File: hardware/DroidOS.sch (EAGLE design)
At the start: 17 parts, among them J1 AUDIO_JACK_3.5MM_KIT, Q1 BC337

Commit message: Changed layout
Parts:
- J1: value AUDIO_JACK_3.5MM_KIT -> AUDIO_JACK_3.5MM
- U$1: value TEENSY_LC_DIL -> TEENSY_LC
- VREG: value (none) -> 5V
- renumbered + to VBAT+, - to VBAT-
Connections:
- net N$1 renamed DAC_R
- net N$10 renamed AUD_RX
- net N$11 renamed AUD_TX
- net N$12 renamed PWM2_SIG
- net N$13 renamed PWM4_SIG
- net N$14 renamed CTRL_SIG
- net N$15 renamed PWM3_SIG
- net N$16 renamed SBUS_INV_IN
- net N$18 renamed SBUS_INV_OUT
- net N$4 renamed SPK_R
- net N$5 renamed SBUS_OUT
- net N$6 renamed 3V+
- net N$7 renamed SPK_L
- net N$9 renamed PWM1_SIG
- removed net N$2: J1.TSH, U$2.DAC_L
- new net DAC_L: J1.TIP, U$2.DAC_L
- net GND: now also J1.SLEEVE, PWM4.3; no longer J1.RSH

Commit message: v0.3
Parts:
- added PWR_SW: (no value), SparkFun-Connectors:CONN_02
- added R4: (no value), resistor:R-US_R0805
- added STATUS: (no value), led:LEDSML0805
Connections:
- new net N$1: PWR_SW.2, U$1.VIN
- new net N$2: R4.1, STATUS.A
- new net STATUS_LED: R4.2, U$1.21/A7
- net 5V: now also PWR_SW.1; no longer U$1.VIN
- net GND: now also STATUS.C
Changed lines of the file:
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@@
 </variantdefs>
 <classes>
-<class number="0" name="default" width="0.254" drill="0.381">
+<class number="0" name="default" width="0.3556" drill="0.381">
 <clearance class="0" value="0.254"/>
 </class>
@@
 <part name="PWM3" library="SparkFun-Connectors" library_urn="urn:adsk.eagle:library:513" deviceset="CONN_03" device="" package3d_urn="urn:adsk.eagle:package:38063/1"/>
 <part name="SIG_SEL" library="SparkFun-Connectors" library_urn="urn:adsk.eagle:library:513" deviceset="CONN_03" device="" package3d_urn="urn:adsk.eagle:package:38063/1"/>
+<part name="PWR_SW" library="SparkFun-Connectors" library_urn="urn:adsk.eagle:library:513" deviceset="CONN_02" device="" package3d_urn="urn:adsk.eagle:package:38039/1"/>
+<part name="STATUS" library="led" library_urn="urn:adsk.eagle:library:259" deviceset="LED" device="SML0805" package3d_urn="urn:adsk.eagle:package:15830/1"/>
+<part name="GND4" library="supply1" library_urn="urn:adsk.eagle:library:371" deviceset="GND" device=""/>
+<part name="R4" library="resistor" library_urn="urn:adsk.eagle:library:348" deviceset="R-US_" device="R0805" package3d_urn="urn:adsk.eagle:package:26059/1"/>
 </parts>
 <sheets>
@@
 <instance part="PWM3" gate="J$1" x="55.88" y="27.94" rot="R180"/>
 <instance part="SIG_SEL" gate="J$1" x="71.12" y="27.94" rot="R180"/>
+<instance part="PWR_SW" gate="G$1" x="-66.04" y="17.78"/>
+<instance part="STATUS" gate="G$1" x="17.78" y="111.76" rot="R90"/>
+<instance part="GND4" gate="1" x="30.48" y="111.76" rot="R90"/>
+<instance part="R4" gate="G$1" x="7.62" y="111.76" rot="R180"/>
 </instances>
 <busses>
@@
 <wire x1="104.14" y1="88.9" x2="104.14" y2="83.82" width="0.1524" layer="91"/>
 </segment>
+<segment>
+<pinref part="STATUS" gate="G$1" pin="C"/>
+<pinref part="GND4" gate="1" pin="GND"/>
+<wire x1="22.86" y1="111.76" x2="27.94" y2="111.76" width="0.1524" layer="91"/>
+</segment>
 </net>
 <net name="VBAT" class="1">
@@
 <wire x1="40.64" y1="5.08" x2="22.86" y2="5.08" width="0.1524" layer="91"/>
 <wire x1="22.86" y1="5.08" x2="-55.88" y2="5.08" width="0.1524" layer="91"/>
-<wire x1="-55.88" y1="5.08" x2="-55.88" y2="33.02" width="0.1524" layer="91"/>
-<pinref part="U$1" gate="G$1" pin="VIN"/>
-<wire x1="-55.88" y1="33.02" x2="-50.8" y2="33.02" width="0.1524" layer="91"/>
 <wire x1="22.86" y1="27.94" x2="22.86" y2="5.08" width="0.1524" layer="91"/>
 <junction x="22.86" y="5.08"/>
@@
 <pinref part="PWM2" gate="J$1" pin="2"/>
 <pinref part="PWM3" gate="J$1" pin="2"/>
+<pinref part="PWR_SW" gate="G$1" pin="1"/>
+<wire x1="-58.42" y1="17.78" x2="-55.88" y2="17.78" width="0.1524" layer="91"/>
+<wire x1="-55.88" y1="17.78" x2="-55.88" y2="5.08" width="0.1524" layer="91"/>
 </segment>
 </net>
@@
 </segment>
 </net>
+<net name="N$1" class="0">
+<segment>
+<pinref part="PWR_SW" gate="G$1" pin="2"/>
+<pinref part="U$1" gate="G$1" pin="VIN"/>
+<wire x1="-58.42" y1="20.32" x2="-50.8" y2="20.32" width="0.1524" layer="91"/>
+<wire x1="-50.8" y1="20.32" x2="-50.8" y2="33.02" width="0.1524" layer="91"/>
+</segment>
+</net>
+<net name="STATUS_LED" class="0">
+<segment>
+<wire x1="2.54" y1="111.76" x2="0" y2="111.76" width="0.1524" layer="91"/>
+<wire x1="0" y1="111.76" x2="0" y2="83.82" width="0.1524" layer="91"/>
+<pinref part="U$1" gate="G$1" pin="21/A7"/>
+<wire x1="0" y1="83.82" x2="-5.08" y2="83.82" width="0.1524" layer="91"/>
+<pinref part="R4" gate="G$1" pin="2"/>
+</segment>
+</net>
+<net name="N$2" class="0">
+<segment>
+<pinref part="STATUS" gate="G$1" pin="A"/>
+<wire x1="15.24" y1="111.76" x2="12.7" y2="111.76" width="0.1524" layer="91"/>
+<pinref part="R4" gate="G$1" pin="1"/>
+</segment>
+</net>

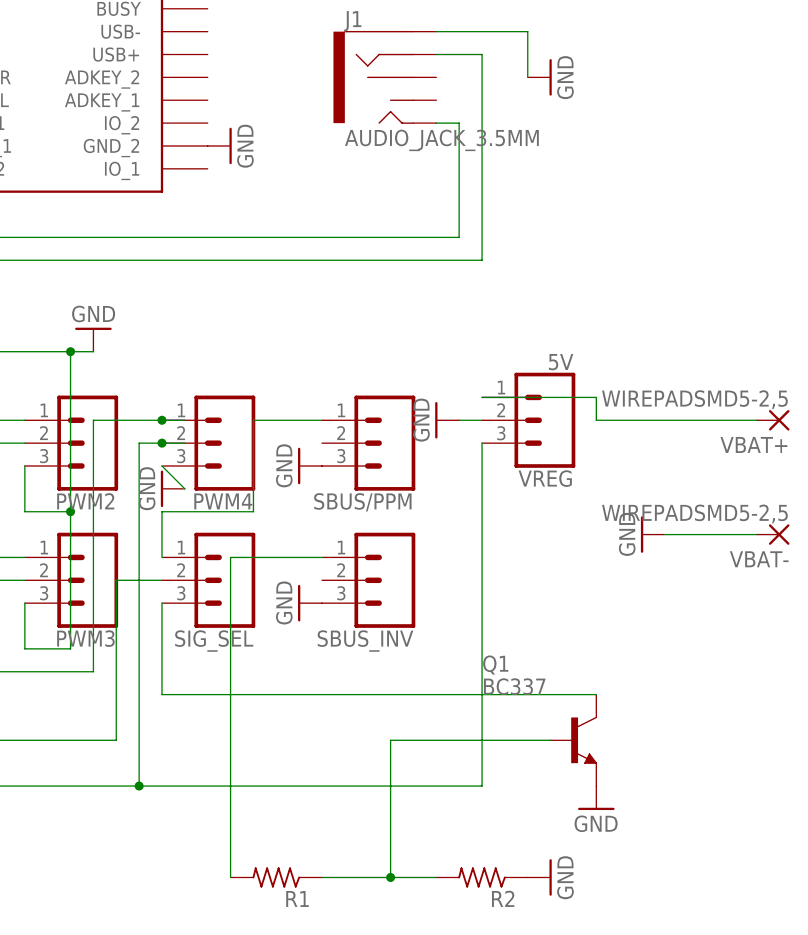
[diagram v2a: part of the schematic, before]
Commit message: Added SBUS power out
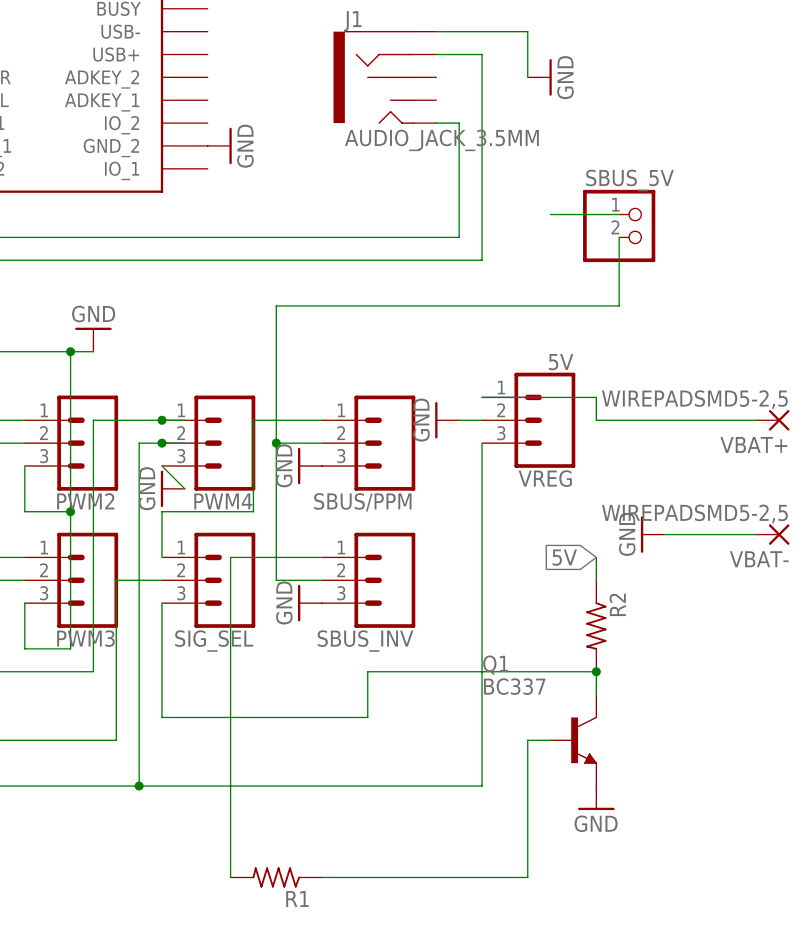
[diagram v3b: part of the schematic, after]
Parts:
- added SBUS_5V: (no value), pinhead:PINHD-1X2
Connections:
- removed net N$17: Q1.B, R1.1, R2.2
- new net N$3: SBUS/PPM.2, SBUS_5V.2, SBUS_INV.2
- new net N$4: Q1.B, R1.1
- net 5V: now also R2.1, SBUS_5V.1
- net GND: no longer R2.1
- net SBUS_INV_OUT: now also R2.2
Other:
- moved on the sheet: R2
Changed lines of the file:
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@@
 <?xml version="1.0" encoding="utf-8"?>
 <!DOCTYPE eagle SYSTEM "eagle.dtd">
-<eagle version="8.4.0">
+<eagle version="8.4.3">
 <drawing>
 <settings>
@@
 <part name="R2" library="resistor" library_urn="urn:adsk.eagle:library:348" deviceset="R-US_" device="R0805" package3d_urn="urn:adsk.eagle:package:26059/1"/>
 <part name="Q1" library="transistor-npn" library_urn="urn:adsk.eagle:library:398" deviceset="BC337*" device="" package3d_urn="urn:adsk.eagle:package:28974/2"/>
-<part name="GND9" library="supply1" library_urn="urn:adsk.eagle:library:371" deviceset="GND" device=""/>
 <part name="GND15" library="supply1" library_urn="urn:adsk.eagle:library:371" deviceset="GND" device=""/>
 <part name="VBAT+" library="wirepad" library_urn="urn:adsk.eagle:library:412" deviceset="WIREPAD" device="SMD5-2,5" package3d_urn="urn:adsk.eagle:package:30845/1"/>
@@
 <part name="GND4" library="supply1" library_urn="urn:adsk.eagle:library:371" deviceset="GND" device=""/>
 <part name="R4" library="resistor" library_urn="urn:adsk.eagle:library:348" deviceset="R-US_" device="R0805" package3d_urn="urn:adsk.eagle:package:26059/1"/>
+<part name="SBUS_5V" library="pinhead" library_urn="urn:adsk.eagle:library:325" deviceset="PINHD-1X2" device="" package3d_urn="urn:adsk.eagle:package:22435/2"/>
 </parts>
 <sheets>
@@
 <instance part="GND8" gate="1" x="78.74" y="25.4" rot="R270"/>
 <instance part="R1" gate="G$1" x="76.2" y="-5.08" rot="R180"/>
-<instance part="R2" gate="G$1" x="99.06" y="-5.08" rot="R180"/>
+<instance part="R2" gate="G$1" x="111.76" y="22.86" rot="R270"/>
 <instance part="Q1" gate="G$1" x="109.22" y="10.16"/>
-<instance part="GND9" gate="1" x="106.68" y="-5.08" rot="R90"/>
 <instance part="GND15" gate="1" x="111.76" y="2.54"/>
 <instance part="VBAT+" gate="G$1" x="132.08" y="45.72" rot="R180"/>
@@
 <instance part="GND4" gate="1" x="30.48" y="111.76" rot="R90"/>
 <instance part="R4" gate="G$1" x="7.62" y="111.76" rot="R180"/>
+<instance part="SBUS_5V" gate="G$1" x="116.84" y="66.04"/>
 </instances>
 <busses>
@@
 <pinref part="GND12" gate="1" pin="GND"/>
 <wire x1="-48.26" y1="40.64" x2="-50.8" y2="40.64" width="0.1524" layer="91"/>
-</segment>
-<segment>
-<pinref part="R2" gate="G$1" pin="1"/>
-<pinref part="GND9" gate="1" pin="GND"/>
 </segment>
 <segment>
@@
 <wire x1="-55.88" y1="17.78" x2="-55.88" y2="5.08" width="0.1524" layer="91"/>
 </segment>
+<segment>
+<pinref part="SBUS_5V" gate="G$1" pin="1"/>
+<wire x1="114.3" y1="68.58" x2="106.68" y2="68.58" width="0.1524" layer="91"/>
+</segment>
+<segment>
+<pinref part="R2" gate="G$1" pin="1"/>
+<wire x1="111.76" y1="27.94" x2="111.76" y2="30.48" width="0.1524" layer="91"/>
+<label x="111.76" y="30.48" size="1.778" layer="95" rot="R180" xref="yes"/>
+</segment>
 </net>
 <net name="PWM1_SIG" class="0">
@@
 </segment>
 </net>
-<net name="N$17" class="0">
-<segment>
-<pinref part="R1" gate="G$1" pin="1"/>
+<net name="SBUS_INV_OUT" class="0">
+<segment>
+<wire x1="63.5" y1="12.7" x2="63.5" y2="25.4" width="0.1524" layer="91"/>
+<pinref part="SIG_SEL" gate="J$1" pin="3"/>
 <pinref part="R2" gate="G$1" pin="2"/>
-<wire x1="81.28" y1="-5.08" x2="88.9" y2="-5.08" width="0.1524" layer="91"/>
-<wire x1="88.9" y1="-5.08" x2="93.98" y2="-5.08" width="0.1524" layer="91"/>
-<wire x1="88.9" y1="-5.08" x2="88.9" y2="10.16" width="0.1524" layer="91"/>
-<junction x="88.9" y="-5.08"/>
-<pinref part="Q1" gate="G$1" pin="B"/>
-<wire x1="88.9" y1="10.16" x2="106.68" y2="10.16" width="0.1524" layer="91"/>
-</segment>
-</net>
-<net name="SBUS_INV_OUT" class="0">
-<segment>
 <pinref part="Q1" gate="G$1" pin="C"/>
-<wire x1="111.76" y1="15.24" x2="63.5" y2="15.24" width="0.1524" layer="91"/>
-<wire x1="63.5" y1="15.24" x2="63.5" y2="25.4" width="0.1524" layer="91"/>
-<pinref part="SIG_SEL" gate="J$1" pin="3"/>
+<wire x1="111.76" y1="17.78" x2="111.76" y2="15.24" width="0.1524" layer="91"/>
+<wire x1="111.76" y1="17.78" x2="86.36" y2="17.78" width="0.1524" layer="91"/>
+<junction x="111.76" y="17.78"/>
+<wire x1="86.36" y1="17.78" x2="86.36" y2="12.7" width="0.1524" layer="91"/>
+<wire x1="86.36" y1="12.7" x2="63.5" y2="12.7" width="0.1524" layer="91"/>
 </segment>
 </net>
@@
 </segment>
 </net>
+<net name="N$3" class="0">
+<segment>
+<pinref part="SBUS_5V" gate="G$1" pin="2"/>
+<wire x1="114.3" y1="66.04" x2="114.3" y2="58.42" width="0.1524" layer="91"/>
+<wire x1="114.3" y1="58.42" x2="76.2" y2="58.42" width="0.1524" layer="91"/>
+<pinref part="SBUS/PPM" gate="J$1" pin="2"/>
+<wire x1="76.2" y1="58.42" x2="76.2" y2="43.18" width="0.1524" layer="91"/>
+<wire x1="76.2" y1="43.18" x2="81.28" y2="43.18" width="0.1524" layer="91"/>
+<pinref part="SBUS_INV" gate="J$1" pin="2"/>
+<wire x1="81.28" y1="27.94" x2="76.2" y2="27.94" width="0.1524" layer="91"/>
+<wire x1="76.2" y1="27.94" x2="76.2" y2="43.18" width="0.1524" layer="91"/>
+<junction x="76.2" y="43.18"/>
+</segment>
+</net>
+<net name="N$4" class="0">
+<segment>
+<pinref part="R1" gate="G$1" pin="1"/>
+<wire x1="81.28" y1="-5.08" x2="104.14" y2="-5.08" width="0.1524" layer="91"/>
+<pinref part="Q1" gate="G$1" pin="B"/>
+<wire x1="104.14" y1="-5.08" x2="104.14" y2="10.16" width="0.1524" layer="91"/>
+<wire x1="104.14" y1="10.16" x2="106.68" y2="10.16" width="0.1524" layer="91"/>
+</segment>
+</net>
